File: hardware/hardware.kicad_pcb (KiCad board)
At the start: 2 copper layers, 60 x 80 mm, 6 parts, among them J1 USB_C_Receptacle_USB2.0_14P, J3 Conn_01x08_Socket, U2 ESP32-S3-WROOM-1

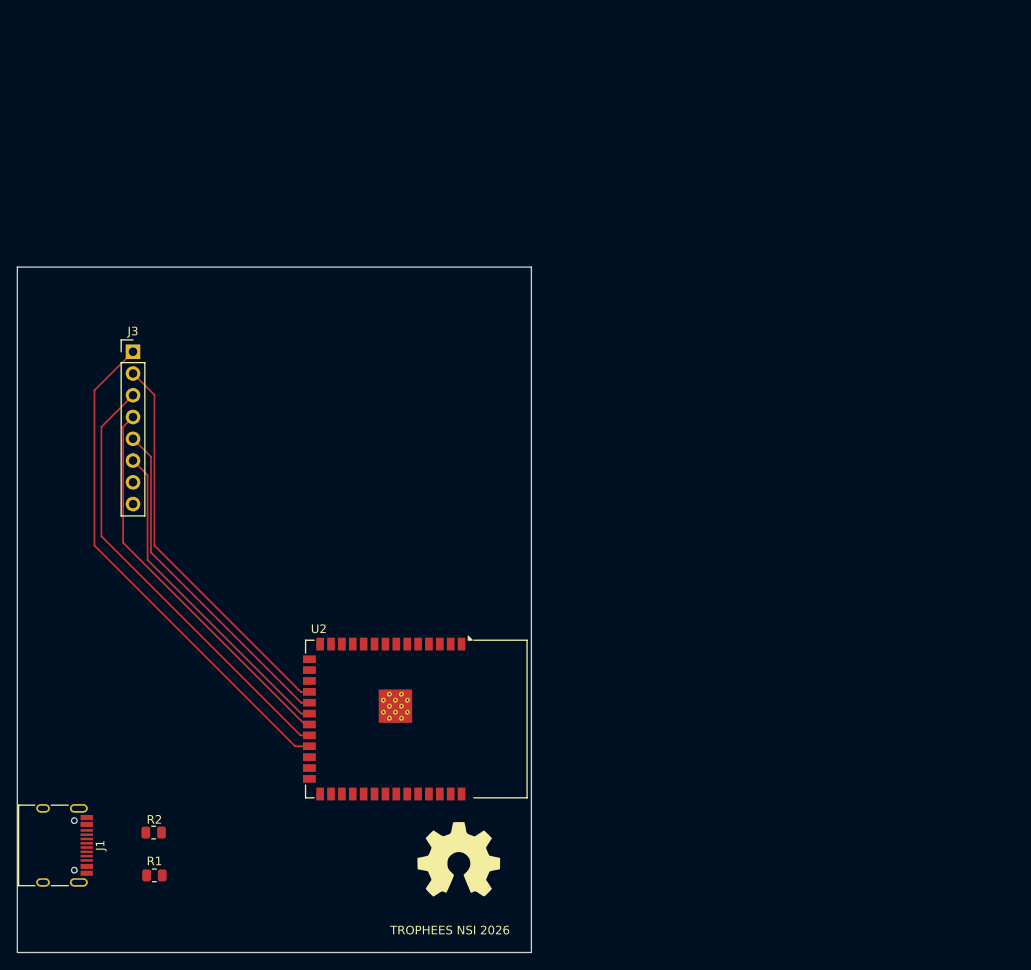
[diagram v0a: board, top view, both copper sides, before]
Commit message: Adding usbc routes [ERC NOT STABLE]
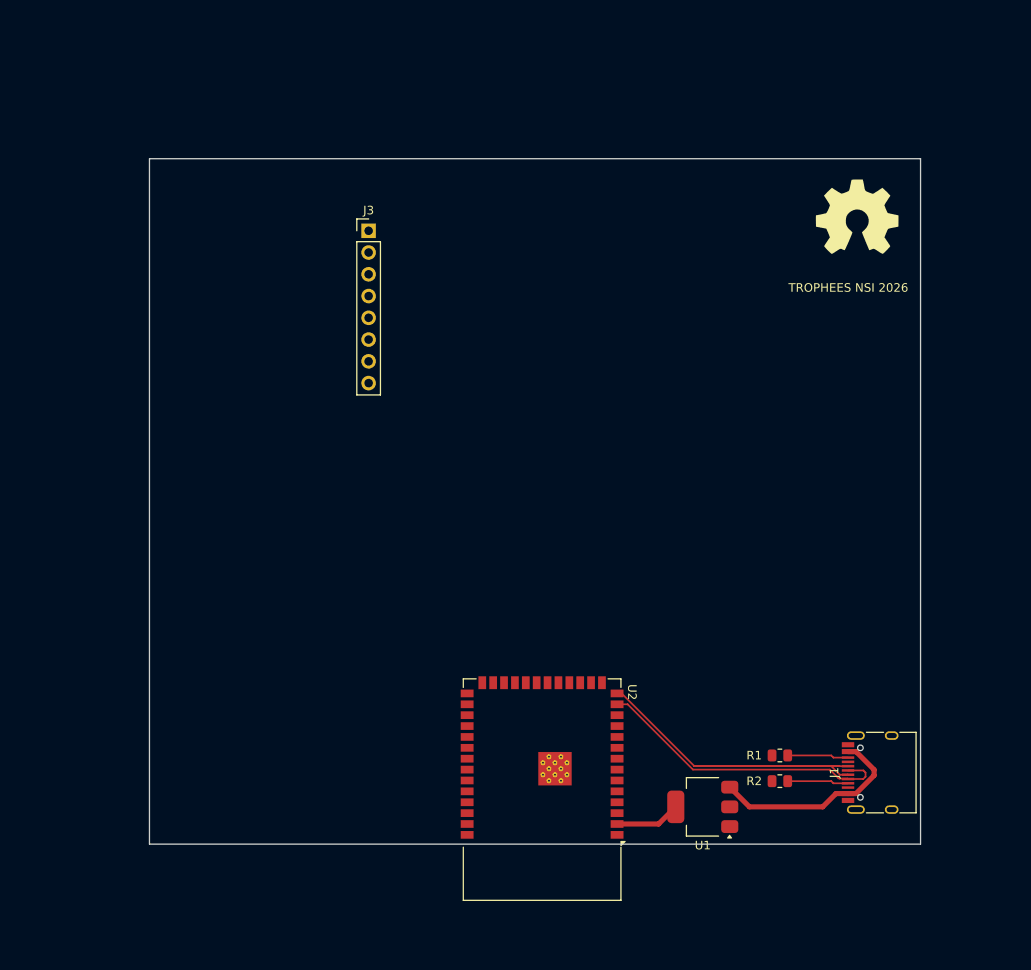
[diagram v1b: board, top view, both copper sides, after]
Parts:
- added U1: AMS1117-3.3, Package_TO_SOT_SMD:SOT-223-3_TabPin2, F.Cu at (205.0, 118.0)
- moved J1 97.3 mm to (226.0, 114.0), turned to 90 degrees
- moved G*** 88.2 mm to (223.0, 49.0)
- moved R1 74.3 mm to (214.0, 112.0), turned to 180 degrees
- moved R2 73.3 mm to (214.0, 115.0), turned to 180 degrees
- moved J3 30.9 mm to (166.0, 50.8)
- moved U2 16.8 mm to (186.2, 116.0), turned to 180 degrees
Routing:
- net BLK: track 59.3 -> 0.00 mm
- net DC: track 51.9 -> 0.00 mm
- net DATA+: track 0.00 -> 49.8 mm
- net CS: track 46.3 -> 0.00 mm
- net RES: track 45.7 -> 0.00 mm
- net MOSI: track 39.9 -> 0.00 mm
- net SCLK: track 38.6 -> 0.00 mm
- net DATA-: track 0.00 -> 35.4 mm
- net +5V: track 0.00 -> 23.9 mm
- net +3V3: track 0.00 -> 7.68 mm
- net Net-(J1-CC2): track 0.00 -> 7.15 mm
- net Net-(J1-CC1): track 0.00 -> 7.15 mm
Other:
- board size 60 x 80 mm -> 90 x 80 mm

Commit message: Adding DHT sensor pins
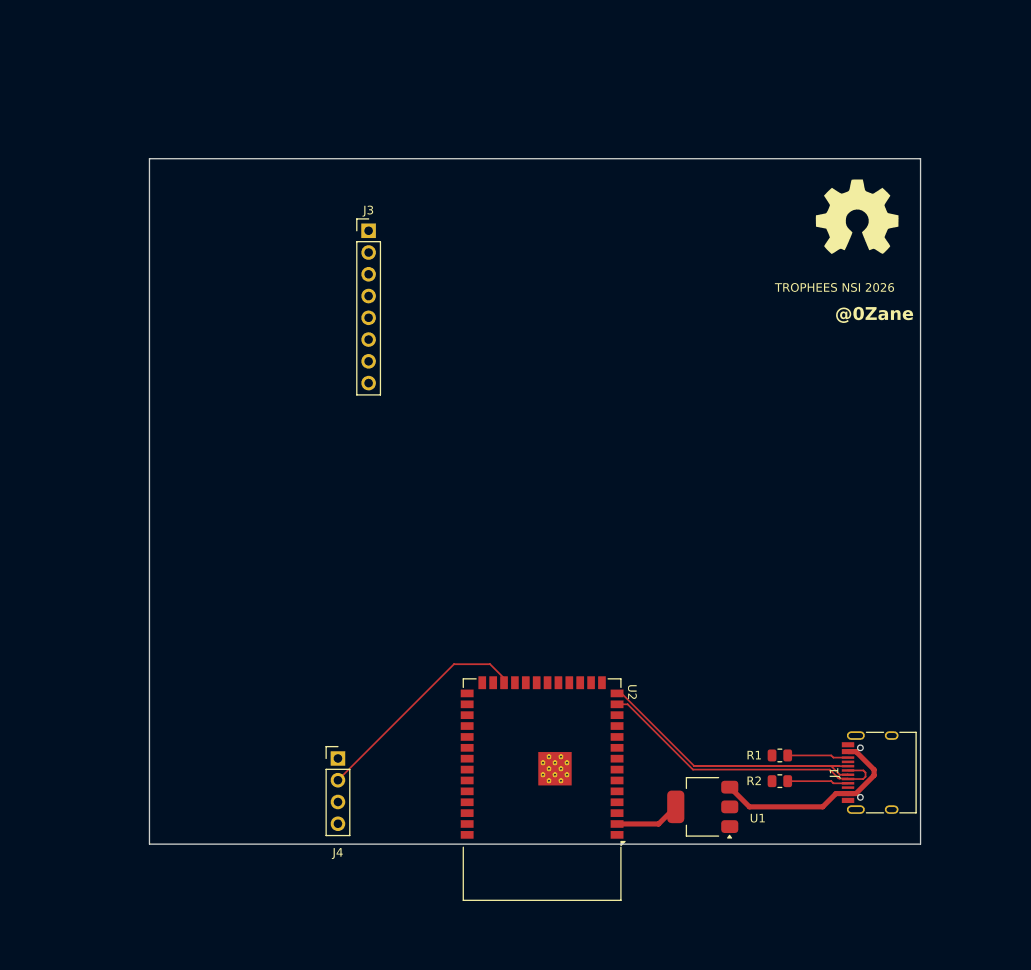
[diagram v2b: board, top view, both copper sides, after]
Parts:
- added J4: Conn_01x04_Socket, Connector_PinHeader_2.54mm:PinHeader_1x04_P2.54mm_Vertical, F.Cu at (162.4, 112.3)
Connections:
- U2 pad 24: unconnected-(U2-IO47-Pad24) -> DHT11
- U2 pad 8: unconnected-(U2-IO15-Pad8) -> DHT11
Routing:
- net DHT11: track 0.00 -> 26.2 mm
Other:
- board text added: "@0Zane"

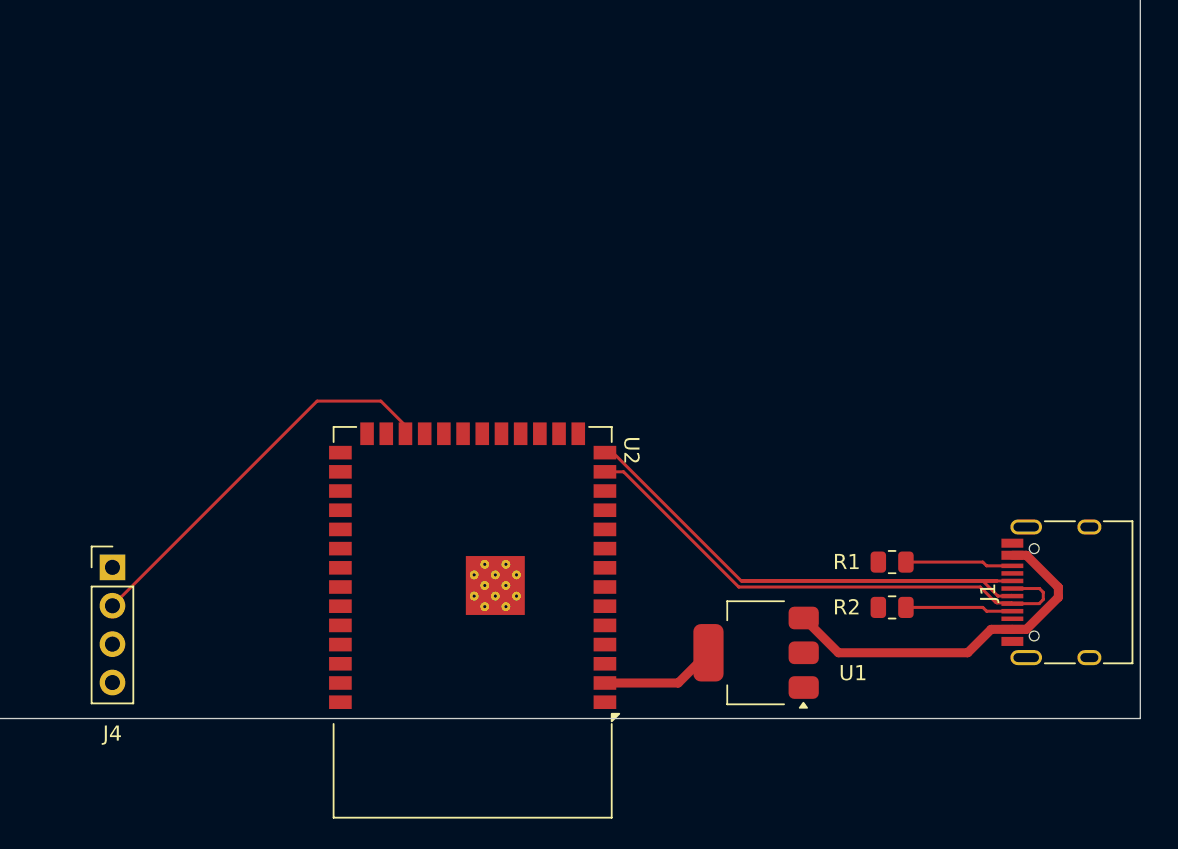
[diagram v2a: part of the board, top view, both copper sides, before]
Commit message: Adding Soil sensor on PCB
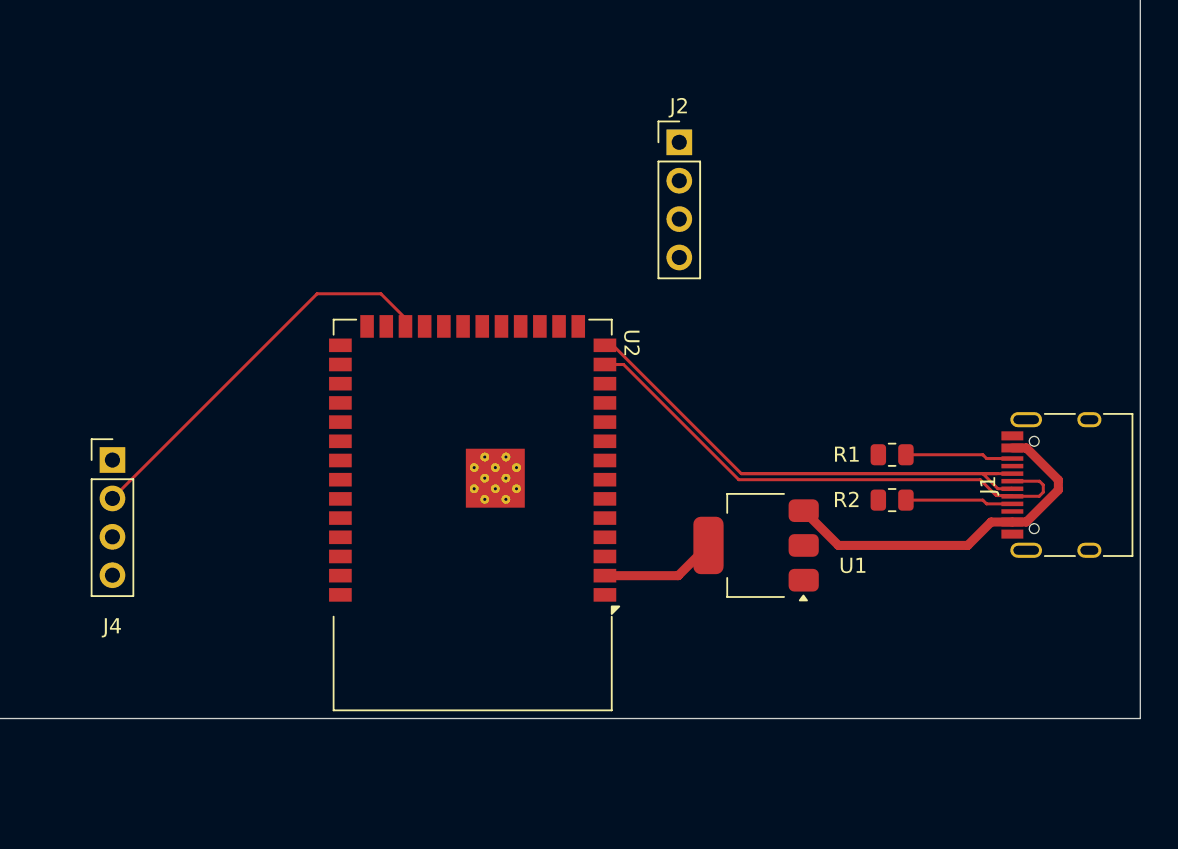
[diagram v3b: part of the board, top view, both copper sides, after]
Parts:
- added J2: Conn_01x04_Socket, Connector_PinHeader_2.54mm:PinHeader_1x04_P2.54mm_Vertical, F.Cu at (199.9, 84.2)
- moved U2 7.10 mm to (186.2, 108.9)
- moved J1 7.10 mm to (226.0, 106.9)
- moved J4 7.10 mm to (162.4, 105.2)
- moved R1 7.10 mm to (214.0, 104.9)
- moved R2 7.10 mm to (214.0, 107.9)
- moved U1 7.10 mm to (205.0, 110.9)
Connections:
- U2 pad 11: unconnected-(U2-IO18-Pad11) -> AO_SOIL
- U2 pad 24: DHT11 -> unconnected-(U2-IO47-Pad24)
- U2 pad 8: DHT11 -> unconnected-(U2-IO15-Pad8)
- U2 pad 9: unconnected-(U2-IO16-Pad9) -> DHT11

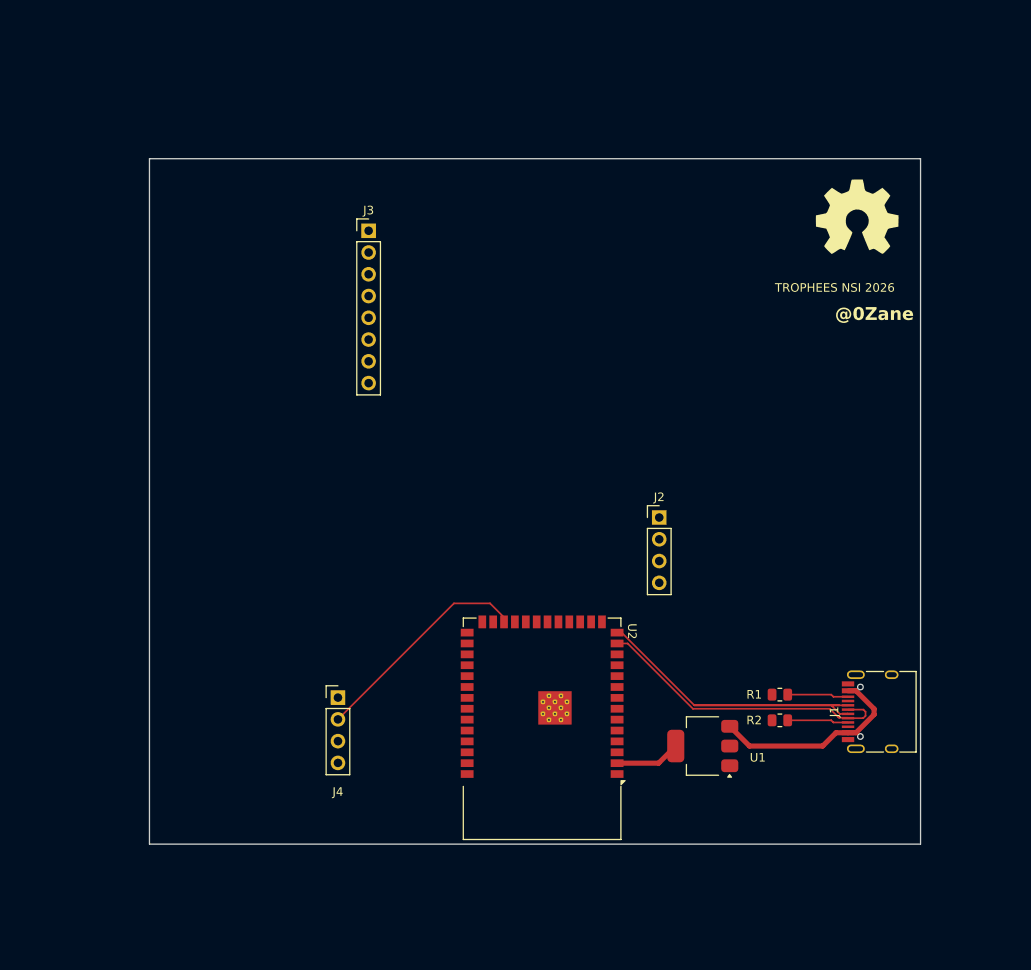
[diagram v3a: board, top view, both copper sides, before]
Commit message: Making first version of the PCB [NOT ROUTED ]
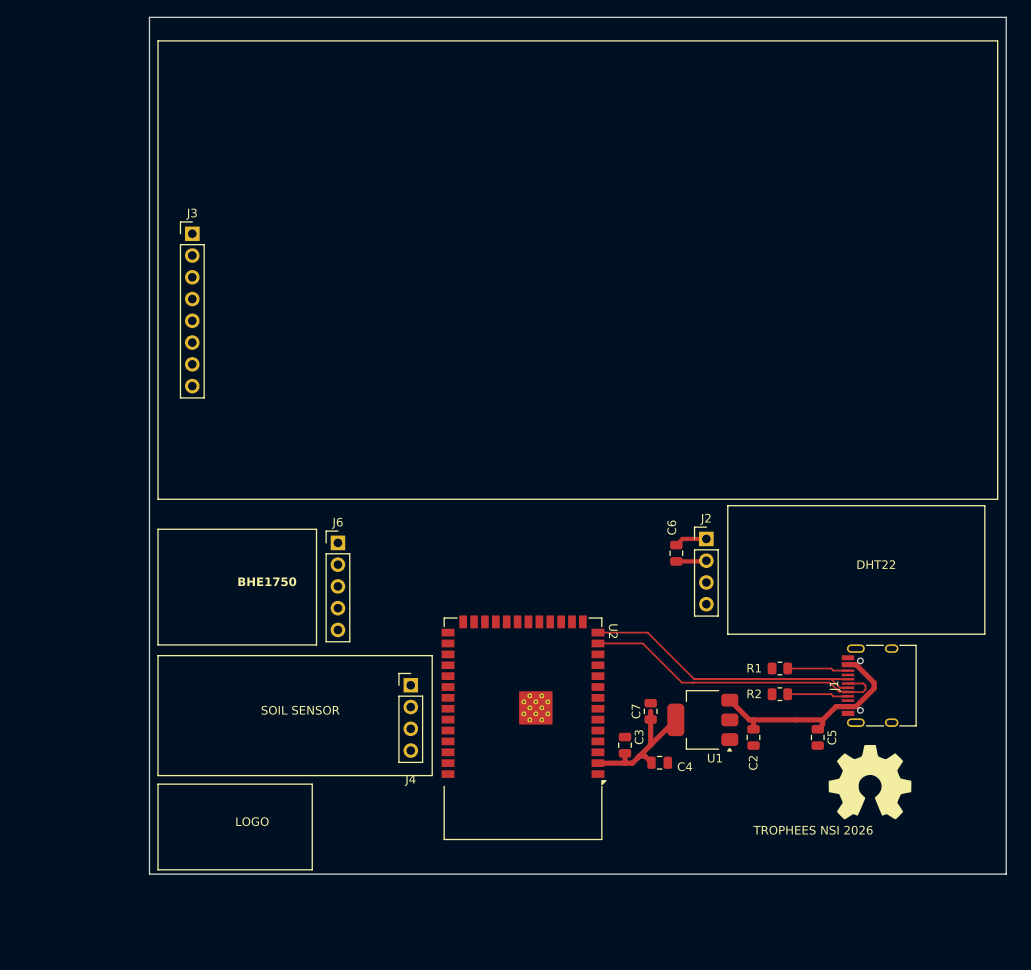
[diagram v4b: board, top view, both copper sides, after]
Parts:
- added C2: 10uF, Capacitor_SMD:C_0805_2012Metric, F.Cu at (210.9, 109.9)
- added C3: 0.1uF, Capacitor_SMD:C_0805_2012Metric, F.Cu at (195.9, 110.8)
- added C4: 22uF, Capacitor_SMD:C_0805_2012Metric, F.Cu at (200.0, 112.8)
- added C5: 10nF, Capacitor_SMD:C_0805_2012Metric, F.Cu at (218.4, 109.9)
- added C6: 0.1uF, Capacitor_SMD:C_0805_2012Metric, F.Cu at (201.9, 88.4)
- added C7: 22uF, Capacitor_SMD:C_0805_2012Metric, F.Cu at (198.9, 106.8)
- added J6: Conn_01x05_Socket, Connector_PinHeader_2.54mm:PinHeader_1x05_P2.54mm_Vertical, F.Cu at (162.4, 87.2)
- moved G*** 66.0 mm to (224.5, 115.0)
- moved J3 20.6 mm to (145.4, 51.1)
- moved J4 8.62 mm to (170.9, 103.8)
- moved J2 6.04 mm to (205.4, 86.7)
- moved J1 3.05 mm to (226.0, 103.8)
- moved R1 3.05 mm to (214.0, 101.8)
- moved R2 3.05 mm to (214.0, 104.8)
- moved U1 3.05 mm to (205.0, 107.8)
- moved U2 2.23 mm to (184.0, 108.9)
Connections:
- U2 pad 23: BLK -> unconnected-(U2-IO21-Pad23)
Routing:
- net DHT11: track 26.2 -> 0.00 mm
- net +3V3: track 7.68 -> 22.2 mm
- net GND: track 0.00 -> 3.53 mm
- net +5V: track 23.9 -> 26.3 mm
- net DATA-: track 35.4 -> 36.4 mm
- net DATA+: track 49.8 -> 50.8 mm
- net DC: track 0.00 -> 0.53 mm
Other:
- board size 90 x 80 mm -> 100 x 100 mm
- board text added: "BHE1750"
- board text added: "DHT22"
- board text added: "LOGO"
- board text added: "SOIL SENSOR"
- board text removed: "@0Zane"

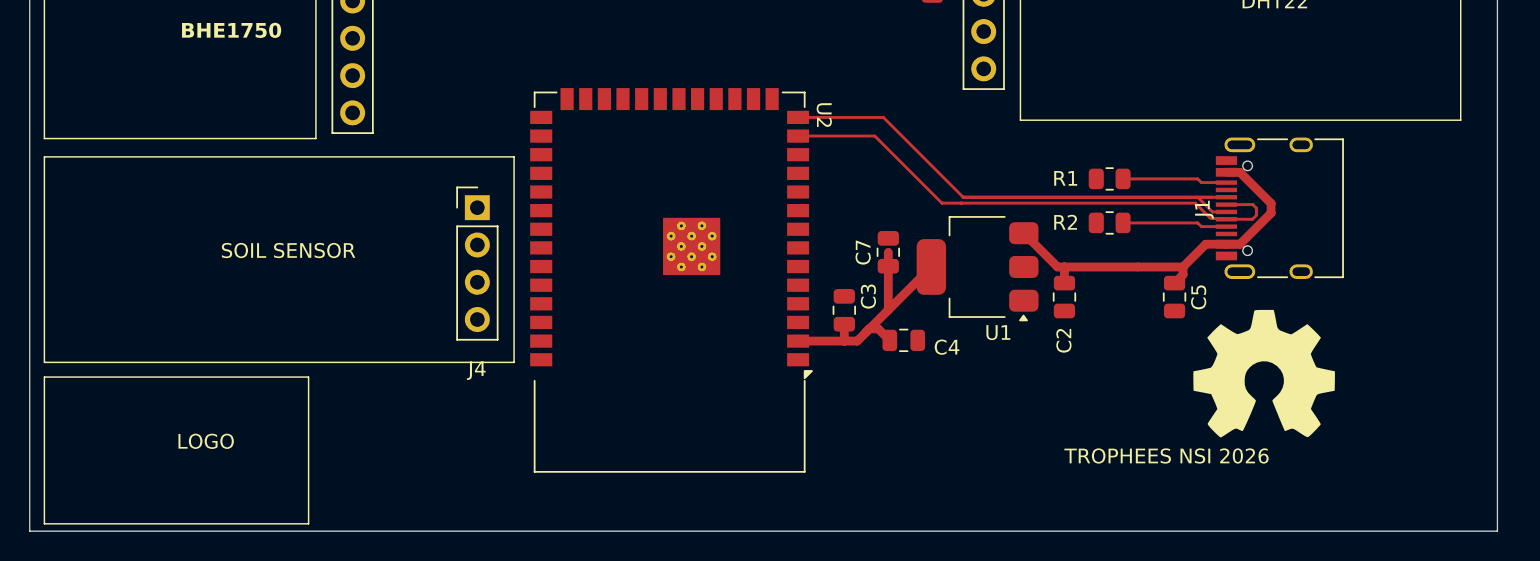
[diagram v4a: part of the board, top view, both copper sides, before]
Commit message: Placing silkscreen in better zones to preapare mounting holes
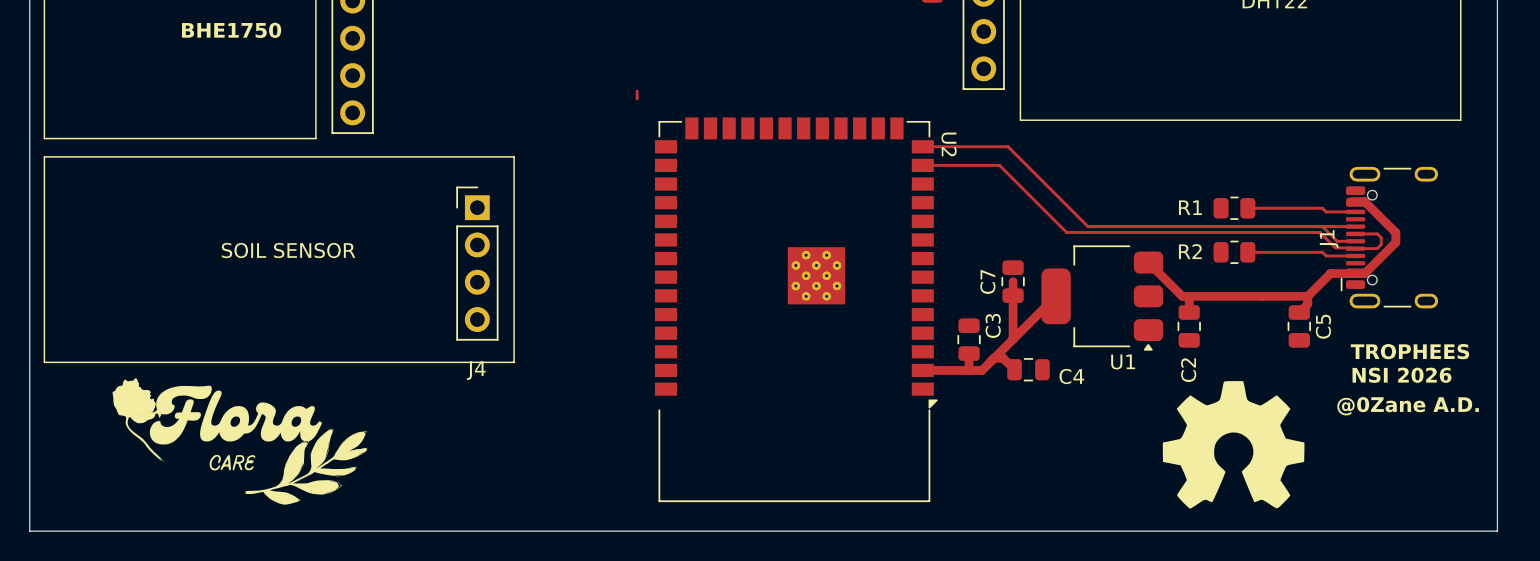
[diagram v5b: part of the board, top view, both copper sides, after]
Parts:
- added G***: LOGO, LOGO, F.Cu at (154.4, 119.8)
- J1: footprint Connector_USB:USB_C_Receptacle_HRO_TYPE-C-31-M-12 -> Connector_USB:USB_C_Receptacle_HCTL_HC-TYPE-C-16P-01A
- moved C2 8.73 mm to (219.4, 111.9)
- moved C3 8.73 mm to (204.4, 112.8)
- moved C4 8.73 mm to (208.5, 114.8)
- moved C5 8.73 mm to (226.9, 111.9)
- moved C7 8.73 mm to (207.4, 108.8)
- moved J1 8.73 mm to (234.5, 105.8)
- moved R1 8.73 mm to (222.5, 103.8)
- moved R2 8.73 mm to (222.5, 106.8)
- moved U1 8.73 mm to (213.5, 109.8)
- moved U2 8.73 mm to (192.5, 110.9)
- moved G*** 5.28 mm to (222.4, 119.8)
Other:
- board text added: "@0Zane A.D."
- board text removed: "LOGO"
